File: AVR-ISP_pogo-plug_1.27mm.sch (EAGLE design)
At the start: 1 part

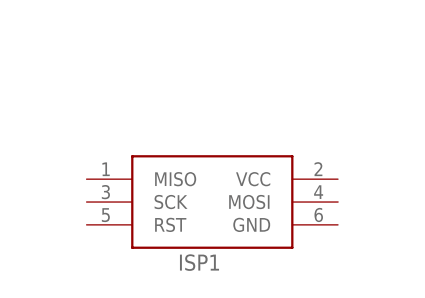
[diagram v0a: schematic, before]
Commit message: done, fliped pins from source.
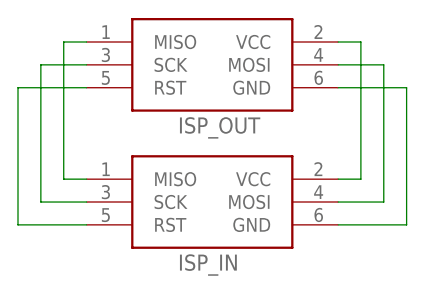
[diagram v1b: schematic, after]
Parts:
- added ISP_OUT: AVRISPPOGOPINS, TinyTony_ShenzenReady:AVRISPPOGOPINS
- ISP_IN: SPICEPREFIX (none) -> X
- renumbered ISP1 to ISP_IN
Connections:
- new net N$1: ISP_IN.VCC, ISP_OUT.VCC
- new net N$2: ISP_IN.MOSI, ISP_OUT.MOSI
- new net N$3: ISP_IN.GND, ISP_OUT.GND
- new net N$4: ISP_IN.MISO, ISP_OUT.MISO
- new net N$5: ISP_IN.SCK, ISP_OUT.SCK
- new net N$6: ISP_IN.RST, ISP_OUT.RST
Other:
- note added: "https://github.com/shenkarSElab/AVR-ISP_pogo-plug_1.27mm [eagle fork]"
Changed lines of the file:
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@@
 <grid distance="0.1" unitdist="inch" unit="inch" style="lines" multiple="1" display="no" altdistance="0.01" altunitdist="inch" altunit="inch"/>
 <layers>
-<layer number="1" name="Top" color="4" fill="1" visible="no" active="no"/>
-<layer number="16" name="Bottom" color="1" fill="1" visible="no" active="no"/>
-<layer number="17" name="Pads" color="2" fill="1" visible="no" active="no"/>
-<layer number="18" name="Vias" color="2" fill="1" visible="no" active="no"/>
-<layer number="19" name="Unrouted" color="6" fill="1" visible="no" active="no"/>
-<layer number="20" name="Dimension" color="15" fill="1" visible="no" active="no"/>
-<layer number="21" name="tPlace" color="7" fill="1" visible="no" active="no"/>
-<layer number="22" name="bPlace" color="7" fill="1" visible="no" active="no"/>
-<layer number="23" name="tOrigins" color="15" fill="1" visible="no" active="no"/>
-<layer number="24" name="bOrigins" color="15" fill="1" visible="no" active="no"/>
-<layer number="25" name="tNames" color="7" fill="1" visible="no" active="no"/>
-<layer number="26" name="bNames" color="7" fill="1" visible="no" active="no"/>
-<layer number="27" name="tValues" color="7" fill="1" visible="no" active="no"/>
-<layer number="28" name="bValues" color="7" fill="1" visible="no" active="no"/>
+<layer number="1" name="Top" color="4" fill="1" visible="yes" active="no"/>
+<layer number="16" name="Bottom" color="1" fill="1" visible="yes" active="no"/>
+<layer number="17" name="Pads" color="2" fill="1" visible="yes" active="no"/>
+<layer number="18" name="Vias" color="2" fill="1" visible="yes" active="no"/>
+<layer number="19" name="Unrouted" color="6" fill="1" visible="yes" active="no"/>
+<layer number="20" name="Dimension" color="24" fill="1" visible="yes" active="no"/>
+<layer number="21" name="tPlace" color="7" fill="1" visible="yes" active="no"/>
+<layer number="22" name="bPlace" color="7" fill="1" visible="yes" active="no"/>
+<layer number="23" name="tOrigins" color="15" fill="1" visible="yes" active="no"/>
+<layer number="24" name="bOrigins" color="15" fill="1" visible="yes" active="no"/>
+<layer number="25" name="tNames" color="7" fill="1" visible="yes" active="no"/>
+<layer number="26" name="bNames" color="7" fill="1" visible="yes" active="no"/>
+<layer number="27" name="tValues" color="7" fill="1" visible="yes" active="no"/>
+<layer number="28" name="bValues" color="7" fill="1" visible="yes" active="no"/>
 <layer number="29" name="tStop" color="7" fill="3" visible="no" active="no"/>
 <layer number="30" name="bStop" color="7" fill="6" visible="no" active="no"/>
@@
 <layer number="35" name="tGlue" color="7" fill="4" visible="no" active="no"/>
 <layer number="36" name="bGlue" color="7" fill="5" visible="no" active="no"/>
-<layer number="37" name="tTest" color="7" fill="1" visible="no" active="no"/>
-<layer number="38" name="bTest" color="7" fill="1" visible="no" active="no"/>
+<layer number="37" name="tTest" color="7" fill="1" visible="yes" active="no"/>
+<layer number="38" name="bTest" color="7" fill="1" visible="yes" active="no"/>
 <layer number="39" name="tKeepout" color="4" fill="11" visible="no" active="no"/>
 <layer number="40" name="bKeepout" color="1" fill="11" visible="no" active="no"/>
@@
 <layer number="44" name="Drills" color="7" fill="1" visible="no" active="no"/>
 <layer number="45" name="Holes" color="7" fill="1" visible="no" active="no"/>
-<layer number="46" name="Milling" color="3" fill="1" visible="no" active="no"/>
-<layer number="47" name="Measures" color="7" fill="1" visible="no" active="no"/>
-<layer number="48" name="Document" color="7" fill="1" visible="no" active="no"/>
-<layer number="49" name="Reference" color="7" fill="1" visible="no" active="no"/>
-<layer number="50" name="dxf" color="7" fill="1" visible="no" active="no"/>
-<layer number="51" name="tDocu" color="7" fill="1" visible="no" active="no"/>
-<layer number="52" name="bDocu" color="7" fill="1" visible="no" active="no"/>
-<layer number="53" name="tGND_GNDA" color="7" fill="1" visible="no" active="no"/>
-<layer number="54" name="bGND_GNDA" color="7" fill="1" visible="no" active="no"/>
-<layer number="56" name="wert" color="7" fill="1" visible="no" active="no"/>
-<layer number="57" name="tCAD" color="7" fill="1" visible="no" active="no"/>
-<layer number="59" name="tCarbon" color="7" fill="1" visible="no" active="no"/>
-<layer number="60" name="bCarbon" color="7" fill="1" visible="no" active="no"/>
+<layer number="46" name="Milling" color="3" fill="1" visible="yes" active="no"/>
+<layer number="47" name="Measures" color="7" fill="1" visible="yes" active="no"/>
+<layer number="48" name="Document" color="7" fill="1" visible="yes" active="no"/>
+<layer number="49" name="Reference" color="7" fill="1" visible="yes" active="no"/>
+<layer number="50" name="dxf" color="7" fill="1" visible="yes" active="no"/>
+<layer number="51" name="tDocu" color="7" fill="1" visible="yes" active="no"/>
+<layer number="52" name="bDocu" color="7" fill="1" visible="yes" active="no"/>
+<layer number="53" name="tGND_GNDA" color="7" fill="1" visible="yes" active="no"/>
+<layer number="54" name="bGND_GNDA" color="7" fill="1" visible="yes" active="no"/>
+<layer number="56" name="wert" color="7" fill="1" visible="yes" active="no"/>
+<layer number="57" name="tCAD" color="7" fill="1" visible="yes" active="no"/>
+<layer number="59" name="tCarbon" color="7" fill="1" visible="yes" active="no"/>
+<layer number="60" name="bCarbon" color="7" fill="1" visible="yes" active="no"/>
 <layer number="88" name="SimResults" color="9" fill="1" visible="yes" active="yes"/>
 <layer number="89" name="SimProbes" color="9" fill="1" visible="yes" active="yes"/>
@@
 <parts>
 <part name="FRAME1" library="TinyTony_ShenzenReady" deviceset="A4L-LOC" device=""/>
-<part name="ISP1" library="TinyTony_ShenzenReady" deviceset="AVRISP" device="-6"/>
+<part name="ISP_IN" library="TinyTony_ShenzenReady" deviceset="AVRISP" device="-6">
+<attribute name="SPICEPREFIX" value="X"/>
+</part>
+<part name="ISP_OUT" library="TinyTony_ShenzenReady" deviceset="AVRISP" device="POGOPINS"/>
 </parts>
 <sheets>
 <sheet>
 <plain>
+<text x="5.08" y="2.54" size="1.778" layer="125">https://github.com/shenkarSElab/AVR-ISP_pogo-plug_1.27mm [eagle fork]</text>
 </plain>
 <instances>
 <instance part="FRAME1" gate="G$1" x="-22.86" y="-22.86"/>
-<instance part="ISP1" gate="G$1" x="58.42" y="48.26"/>
+<instance part="ISP_IN" gate="G$1" x="58.42" y="48.26"/>
+<instance part="ISP_OUT" gate="G$1" x="58.42" y="63.5"/>
 </instances>
 <busses>
 </busses>
 <nets>
+<net name="N$1" class="0">
+<segment>
+<pinref part="ISP_IN" gate="G$1" pin="VCC"/>
+<wire x1="73.66" y1="50.8" x2="76.2" y2="50.8" width="0.1524" layer="91"/>
+<wire x1="76.2" y1="50.8" x2="76.2" y2="66.04" width="0.1524" layer="91"/>
+<pinref part="ISP_OUT" gate="G$1" pin="VCC"/>
+<wire x1="76.2" y1="66.04" x2="73.66" y2="66.04" width="0.1524" layer="91"/>
+</segment>
+</net>
+<net name="N$2" class="0">
+<segment>
+<pinref part="ISP_OUT" gate="G$1" pin="MOSI"/>
+<wire x1="73.66" y1="63.5" x2="78.74" y2="63.5" width="0.1524" layer="91"/>
+<wire x1="78.74" y1="63.5" x2="78.74" y2="48.26" width="0.1524" layer="91"/>
+<pinref part="ISP_IN" gate="G$1" pin="MOSI"/>
+<wire x1="78.74" y1="48.26" x2="73.66" y2="48.26" width="0.1524" layer="91"/>
+</segment>
+</net>
+<net name="N$3" class="0">
+<segment>
+<pinref part="ISP_IN" gate="G$1" pin="GND"/>
+<wire x1="73.66" y1="45.72" x2="81.28" y2="45.72" width="0.1524" layer="91"/>
+<wire x1="81.28" y1="45.72" x2="81.28" y2="60.96" width="0.1524" layer="91"/>
+<pinref part="ISP_OUT" gate="G$1" pin="GND"/>
+<wire x1="81.28" y1="60.96" x2="73.66" y2="60.96" width="0.1524" layer="91"/>
+</segment>
+</net>
+<net name="N$4" class="0">
+<segment>
+<pinref part="ISP_OUT" gate="G$1" pin="MISO"/>
+<wire x1="45.72" y1="66.04" x2="43.18" y2="66.04" width="0.1524" layer="91"/>
+<pinref part="ISP_IN" gate="G$1" pin="MISO"/>
+<wire x1="43.18" y1="66.04" x2="43.18" y2="50.8" width="0.1524" layer="91"/>
+<wire x1="43.18" y1="50.8" x2="45.72" y2="50.8" width="0.1524" layer="91"/>
+</segment>
+</net>
+<net name="N$5" class="0">
+<segment>
+<pinref part="ISP_OUT" gate="G$1" pin="SCK"/>
+<wire x1="45.72" y1="63.5" x2="40.64" y2="63.5" width="0.1524" layer="91"/>
+<pinref part="ISP_IN" gate="G$1" pin="SCK"/>
+<wire x1="40.64" y1="63.5" x2="40.64" y2="48.26" width="0.1524" layer="91"/>
+<wire x1="40.64" y1="48.26" x2="45.72" y2="48.26" width="0.1524" layer="91"/>
+</segment>
+</net>
+<net name="N$6" class="0">
+<segment>
+<pinref part="ISP_IN" gate="G$1" pin="RST"/>
+<wire x1="45.72" y1="45.72" x2="38.1" y2="45.72" width="0.1524" layer="91"/>
+<wire x1="38.1" y1="45.72" x2="38.1" y2="60.96" width="0.1524" layer="91"/>
+<pinref part="ISP_OUT" gate="G$1" pin="RST"/>
+<wire x1="38.1" y1="60.96" x2="45.72" y2="60.96" width="0.1524" layer="91"/>
+</segment>
+</net>
 </nets>
 </sheet>
